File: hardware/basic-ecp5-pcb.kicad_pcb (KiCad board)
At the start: 2 copper layers, 100 x 68 mm, 68 parts, among them J1 Conn_01x02, J2 Conn_02x20_Odd_Even, J3 Conn_02x06_Odd_Even, J4 Conn_02x06_Odd_Even, J5 Conn_02x06_Odd_Even, J6 Conn_02x06_Odd_Even, J7 Conn_02x06_Odd_Even, J8 Conn_02x06_Odd_Even, J9 Conn_02x20_Odd_Even, Q1 Q_NMOS_GSD, SW1 SW_Push, SW2 SW_Push, U1 ECP5U_45_CABGA256, U2 IS25LP016D-JBLE, U3 TLV73312PDBV, U4 TLV73333PDBV, X1 SiT2001B

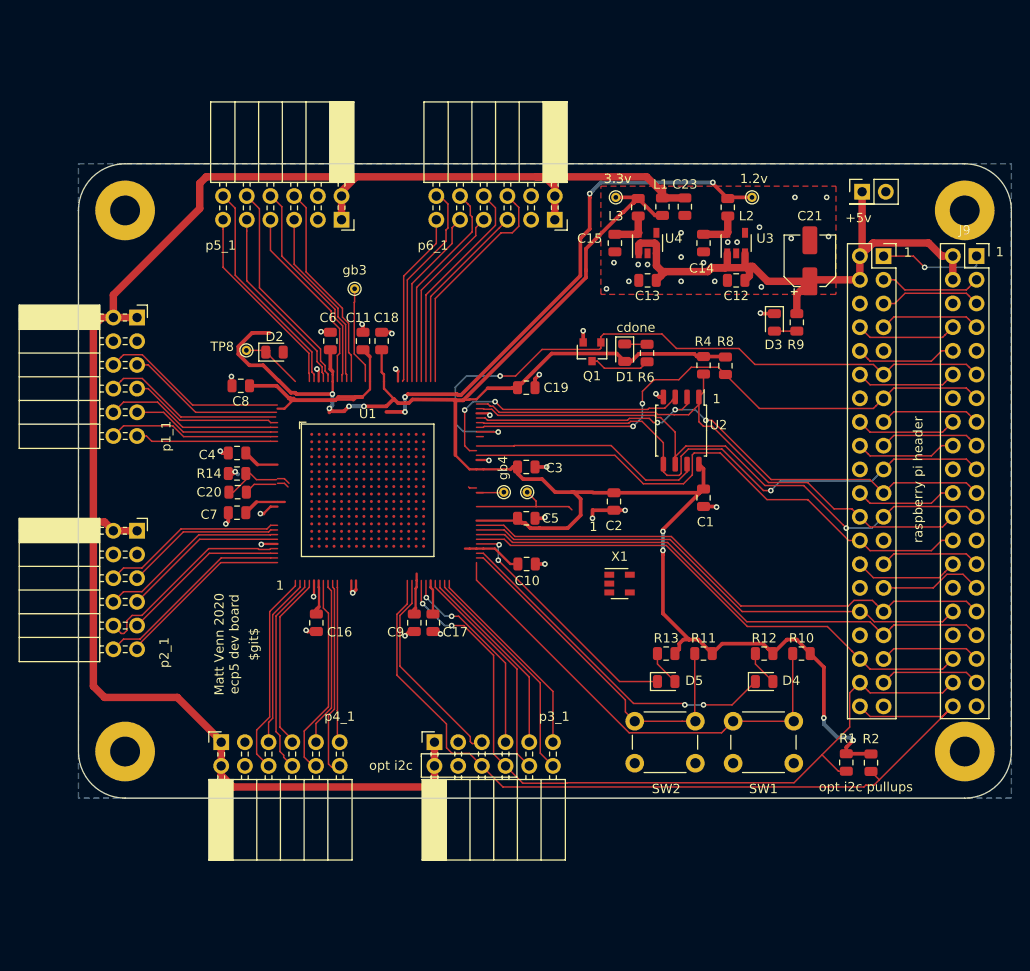
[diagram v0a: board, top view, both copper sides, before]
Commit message: pmods connected and routed
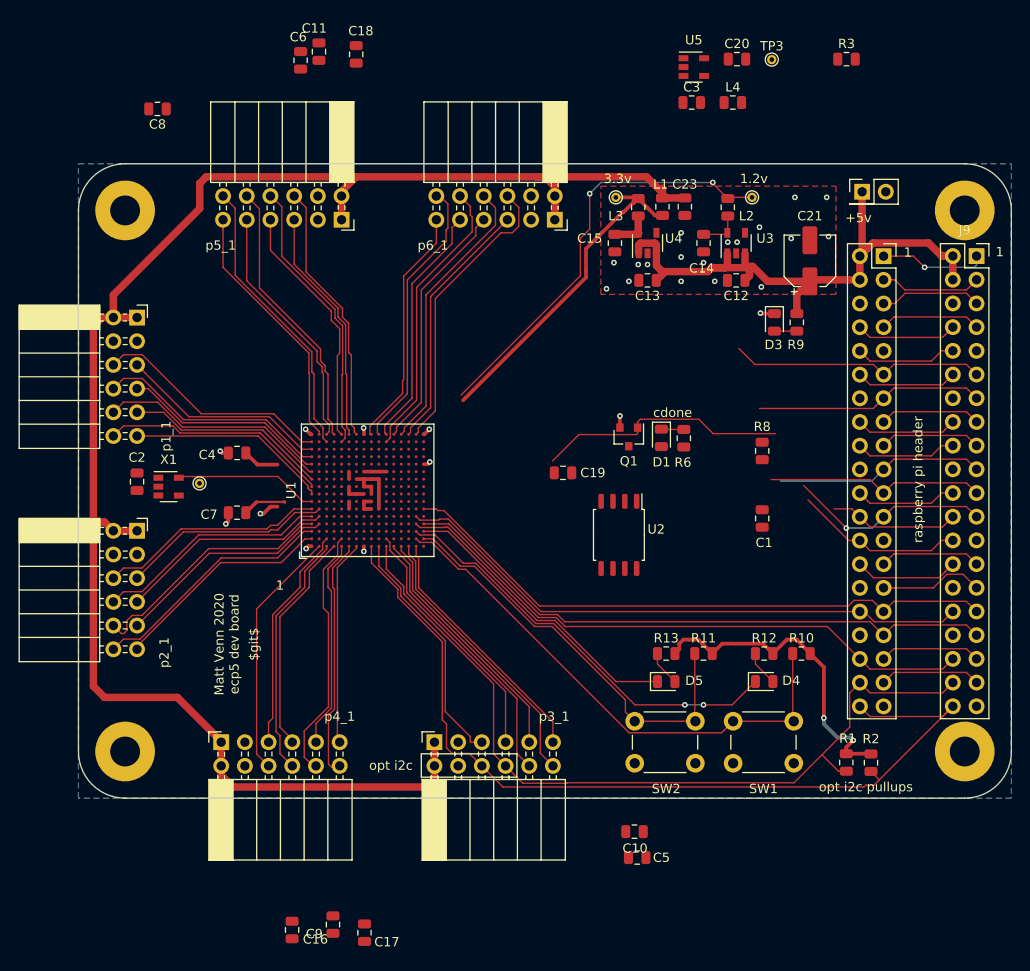
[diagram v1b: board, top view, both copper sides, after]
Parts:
- removed D2: D, Diode_SMD:D_0805_2012Metric
- removed R14: 200R, Resistor_SMD:R_0805_2012Metric
- removed R4: 10k, Resistor_SMD:R_0805_2012Metric
- removed TP1: gbin3, TestPoint:TestPoint_THTPad_D1.0mm_Drill0.5mm
- removed TP2: gbin4, TestPoint:TestPoint_THTPad_D1.0mm_Drill0.5mm
- removed TP8: 2.5v, TestPoint:TestPoint_THTPad_D1.0mm_Drill0.5mm
- added L4: L, Inductor_SMD:L_0805_2012Metric, F.Cu at (145.1, 44.4)
- added R3: 10k, Resistor_SMD:R_0805_2012Metric, F.Cu at (157.3, 39.8)
- added TP3: 2.5v, TestPoint:TestPoint_THTPad_D1.0mm_Drill0.5mm, F.Cu at (149.3, 39.8)
- added U5: TLV73325PDBV, Package_TO_SOT_SMD:SOT-23-5, F.Cu at (141.0, 40.6)
- C20, C3: value 100n -> 1u
- TP6: value 1.2v -> 1.1v
- U3: value TLV73312PDBV -> TLV73311PDBV
- moved C20 70.8 mm to (145.6, 39.8)
- moved C2 51.2 mm to (81.3, 85.1), turned to 90 degrees
- moved X1 49.4 mm to (84.7, 85.6)
- moved C3 42.9 mm to (140.7, 44.4)
- moved C5 38.3 mm to (134.9, 125.4)
- moved TP5 35.1 mm to (88.0, 85.3)
- moved C17 34.0 mm to (105.7, 133.4)
- moved C9 33.5 mm to (102.3, 132.6)
- moved C16 33.0 mm to (97.9, 133.1)
- moved C11 31.4 mm to (100.8, 39.0)
- moved C8 31.0 mm to (83.5, 45.1)
- moved C10 30.9 mm to (134.6, 122.6)
- moved C18 30.9 mm to (104.8, 39.3)
- moved C6 30.3 mm to (98.8, 39.9)
- moved U2 13.0 mm to (132.9, 90.8)
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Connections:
- net +1V2 renamed +1V1
- net /1v2 renamed /1v1
- net Net-(D2-Pad1) renamed +2V5
- net Net-(U1-PadM10) renamed /fpga/tdo
- net Net-(U1-PadR11) renamed /fpga/tdi
- net Net-(U1-PadT10) renamed /fpga/tck
- net Net-(U1-PadT11) renamed /fpga/tms
- C20 pad 1: /vcc_pll -> /2v5
- C20 pad 2: Net-(C20-Pad2) -> GND
- C3 pad 1: +3V3 -> +5V
- D4 pad 1: /led1 -> led1
- D5 pad 1: /led2 -> led2
- J2 pad 11: /cdone -> cdone
- J2 pad 13: /creset -> creset
- J2 pad 19: /gp10 -> sdo
- J2 pad 21: /gp9 -> sdi
- J2 pad 23: /gp11 -> sd_clk
- J2 pad 24: /gp8 -> sd_cs
- J2 pad 31: /gp6 -> gp6
- J2 pad 32: /gp12 -> gp12
- J2 pad 33: /gp13 -> gp13
- J2 pad 36: /gp16 -> gp16
- J2 pad 38: /gp20 -> p3_9
- J2 pad 40: /gp21 -> p3_10
- J3 pad 10: /p1_8 -> p1_8
- J3 pad 11: /p1_1 -> p1_1
- J3 pad 12: /p1_7 -> p1_7
- J3 pad 5: /p1_4 -> p1_4
- J3 pad 6: /p1_10 -> p1_10
- J3 pad 7: /p1_3 -> p1_3
- J3 pad 8: /p1_9 -> p1_9
- J3 pad 9: /p1_2 -> p1_2
- J4 pad 10: /p2_8 -> p2_8
- J4 pad 11: /p2_1 -> p2_1
- J4 pad 12: /p2_7 -> p2_7
- J4 pad 5: /p2_4 -> p2_4
- J4 pad 6: /p2_10 -> p2_10
- J4 pad 7: /p2_3 -> p2_3
- J4 pad 8: /p2_9 -> p2_9
- J4 pad 9: /p2_2 -> p2_2
- J5 pad 10: /p3_8 -> p3_8
- J5 pad 11: /p3_1 -> p3_1
- J5 pad 12: /p3_7 -> p3_7
- J5 pad 5: /p3_4 -> p3_4
- J5 pad 6: /gp21 -> p3_10
- J5 pad 7: /p3_3 -> p3_3
- J5 pad 8: /gp20 -> p3_9
- J5 pad 9: /p3_2 -> p3_2
- J6 pad 10: /p4_8 -> p4_8
- J6 pad 11: /p4_1 -> p4_1
- J6 pad 12: /p4_7 -> p4_7
- J6 pad 5: /p4_4 -> p4_4
- J6 pad 6: /p4_10 -> p4_10
- J6 pad 7: /p4_3 -> p4_3
- J6 pad 8: /p4_9 -> p4_9
- J6 pad 9: /p4_2 -> p4_2
- J7 pad 10: /p5_8 -> p5_8
- J7 pad 11: /p5_1 -> p5_1
- J7 pad 12: /p5_7 -> p5_7
- J7 pad 5: /p5_4 -> p5_4
- J7 pad 6: /p5_10 -> p5_10
- J7 pad 7: /p5_3 -> p5_3
- J7 pad 8: /p5_9 -> p5_9
- J7 pad 9: /p5_2 -> p5_2
- J8 pad 10: /p6_8 -> p6_8
- J8 pad 11: /p6_1 -> p6_1
- J8 pad 12: /p6_7 -> p6_7
- J8 pad 5: /p6_4 -> p6_4
- J8 pad 6: /p6_10 -> p6_10
- J8 pad 7: /p6_3 -> p6_3
- J8 pad 8: /p6_9 -> p6_9
- J8 pad 9: /p6_2 -> p6_2
- J9 pad 11: /cdone -> cdone
- J9 pad 13: /creset -> creset
- J9 pad 19: /gp10 -> sdo
- J9 pad 21: /gp9 -> sdi
- J9 pad 23: /gp11 -> sd_clk
- J9 pad 24: /gp8 -> sd_cs
- J9 pad 31: /gp6 -> gp6
- J9 pad 32: /gp12 -> gp12
- J9 pad 33: /gp13 -> gp13
- J9 pad 36: /gp16 -> gp16
- J9 pad 38: /gp20 -> p3_9
- J9 pad 40: /gp21 -> p3_10
- Q1 pad 1: /cdone -> cdone
- R1 pad 2: /gp20 -> p3_9
- R10 pad 1: /button1 -> button1
- R11 pad 1: /button2 -> button2
- R2 pad 2: /gp21 -> p3_10
- R8 pad 1: /creset -> creset
- SW1 pad 1: /button1 -> button1
- SW2 pad 1: /button2 -> button2
- TP5 pad 1: /clock -> clk
- U1 pad A10: Net-(U1-PadA10) -> p1_2
- U1 pad A11: Net-(U1-PadA11) -> p1_8
- U1 pad A12: Net-(U1-PadA12) -> p1_3
- U1 pad A13: Net-(U1-PadA13) -> p1_9
- U1 pad A14: Net-(U1-PadA14) -> p1_4
- U1 pad A15: Net-(U1-PadA15) -> p1_10
- U1 pad A2: Net-(U1-PadA2) -> p2_1
- U1 pad A3: Net-(U1-PadA3) -> p2_7
- U1 pad A4: Net-(U1-PadA4) -> p2_8
- U1 pad A5: Net-(U1-PadA5) -> p2_9
- U1 pad A6: Net-(U1-PadA6) -> p2_10
- U1 pad A7: Net-(U1-PadA7) -> clk
- U1 pad A8: Net-(U1-PadA8) -> p1_1
- U1 pad A9: Net-(U1-PadA9) -> p1_7
- U1 pad B1: Net-(U1-PadB1) -> p4_10
- U1 pad B16: Net-(U1-PadB16) -> p5_1
- U1 pad B4: Net-(U1-PadB4) -> p2_2
- U1 pad B5: Net-(U1-PadB5) -> p2_3
- U1 pad B6: Net-(U1-PadB6) -> p2_4
- U1 pad C1: Net-(U1-PadC1) -> p4_9
- U1 pad C15: Net-(U1-PadC15) -> p5_7
- U1 pad C16: Net-(U1-PadC16) -> p5_2
- U1 pad C2: Net-(U1-PadC2) -> p4_4
- U1 pad D1: Net-(U1-PadD1) -> p4_3
- U1 pad D16: Net-(U1-PadD16) -> p5_8
- U1 pad E1: Net-(U1-PadE1) -> p4_2
- U1 pad E15: Net-(U1-PadE15) -> p5_9
- U1 pad E16: Net-(U1-PadE16) -> p5_3
- U1 pad E2: Net-(U1-PadE2) -> p4_8
- U1 pad F1: Net-(U1-PadF1) -> p4_7
- U1 pad F16: Net-(U1-PadF16) -> p5_4
- U1 pad G1: Net-(U1-PadG1) -> p4_1
- U1 pad G16: Net-(U1-PadG16) -> p5_10
- U1 pad J1: Net-(U1-PadJ1) -> p3_10
- U1 pad J16: Net-(U1-PadJ16) -> p6_1
- U1 pad K1: Net-(U1-PadK1) -> p3_4
- U1 pad K16: Net-(U1-PadK16) -> p6_7
- U1 pad L1: Net-(U1-PadL1) -> p3_9
- U1 pad L15: Net-(U1-PadL15) -> p6_8
- U1 pad L16: Net-(U1-PadL16) -> p6_2
- U1 pad L2: Net-(U1-PadL2) -> p3_3
- U1 pad M1: Net-(U1-PadM1) -> p3_8
- U1 pad M16: Net-(U1-PadM16) -> p6_3
- U1 pad M7: Net-(U1-PadM7) -> sd_io2
- U1 pad N1: Net-(U1-PadN1) -> p3_2
- U1 pad N10: Net-(U1-PadN10) -> GND
- U1 pad N16: Net-(U1-PadN16) -> p6_9
- U1 pad N7: Net-(U1-PadN7) -> sd_io3
- U1 pad N8: Net-(U1-PadN8) -> sd_cs
- U1 pad N9: Net-(U1-PadN9) -> sd_clk
- U1 pad P1: Net-(U1-PadP1) -> p3_7
- U1 pad P10: Net-(U1-PadP10) -> +3V3
- U1 pad P16: Net-(U1-PadP16) -> p6_4
- U1 pad P9: Net-(U1-PadP9) -> cdone
- U1 pad R1: Net-(U1-PadR1) -> p3_1
- U1 pad R10: Net-(U1-PadR10) -> GND
- U1 pad R16: Net-(U1-PadR16) -> p6_10
- U1 pad R2: Net-(U1-PadR2) -> button1
- U1 pad R3: Net-(U1-PadR3) -> led1
- U1 pad R4: Net-(U1-PadR4) -> gp16
- U1 pad R5: Net-(U1-PadR5) -> gp12
- U1 pad R9: Net-(U1-PadR9) -> creset
- U1 pad T2: Net-(U1-PadT2) -> button2
- U1 pad T3: Net-(U1-PadT3) -> led2
- U1 pad T4: Net-(U1-PadT4) -> gp13
- U1 pad T6: Net-(U1-PadT6) -> gp6
- U1 pad T7: Net-(U1-PadT7) -> sdi
- U1 pad T8: Net-(U1-PadT8) -> sdo
- U2 pad 1: /gp8 -> sd_cs
- U2 pad 2: /gp9 -> sdi
- U2 pad 3: /sd_io2 -> sd_io2
- U2 pad 5: /gp10 -> sdo
- U2 pad 6: /gp11 -> sd_clk
- U2 pad 7: /sd_io3 -> sd_io3
- X1 pad 5: /clock -> clk
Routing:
- net +3V3: track 237.8 -> 85.0 mm, vias 8 -> 2
- net p3_10: track 0.00 -> 96.7 mm
- net /gp21: track 92.4 -> 0.00 mm
- net p3_9: track 0.00 -> 88.4 mm
- net /gp20: track 84.4 -> 0.00 mm, vias 2 -> 0
- net /cdone: track 72.9 -> 0.00 mm, vias 2 -> 0
- net gp6: track 0.00 -> 65.2 mm
- net gp13: track 0.00 -> 65.1 mm
- net gp16: track 0.00 -> 64.5 mm
- net /gp11: track 64.4 -> 0.00 mm, vias 1 -> 0
- net /gp10: track 63.9 -> 0.00 mm, vias 1 -> 0
- net gp12: track 0.00 -> 62.8 mm
- net /gp8: track 62.4 -> 0.00 mm
- net /gp9: track 61.5 -> 0.00 mm, vias 3 -> 0
- net /creset: track 61.1 -> 0.00 mm, vias 2 -> 0
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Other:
- net class Default: clearance 0.16 -> 0.15; trace_width 0.16 -> 0.15
- rule trace_clearance: 0.16 -> 0.15
- rule trace_min: 0.16 -> 0.15
- board text removed: "gb3"
- board text removed: "gb4"

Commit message: routed
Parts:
- removed C16, C17, C18, C19, C9: 100n, Capacitor_SMD:C_0805_2012Metric
- added C22: 100n, Capacitor_SMD:C_0805_2012Metric, F.Cu at (99.0, 95.8)
- added C24: 100n, Capacitor_SMD:C_0805_2012Metric, F.Cu at (97.0, 74.2)
- added C25: 100n, Capacitor_SMD:C_0805_2012Metric, F.Cu at (115.8, 74.6)
- added C26: 100n, Capacitor_SMD:C_0805_2012Metric, F.Cu at (114.8, 95.9)
- added J10: Conn_02x05_Odd_Even, Connector_PinHeader_1.27mm:PinHeader_2x05_P1.27mm_Vertical, F.Cu at (122.4, 82.2)
- added R14: 10k, Resistor_SMD:R_0805_2012Metric, F.Cu at (144.0, 80.5)
- added R4: 10k, Resistor_SMD:R_0805_2012Metric, F.Cu at (130.0, 82.1)
- added R5: 10k, Resistor_SMD:R_0805_2012Metric, F.Cu at (125.6, 82.1)
- added R7: 10k, Resistor_SMD:R_0805_2012Metric, F.Cu at (127.8, 82.1)
- moved R3 61.7 mm to (133.8, 96.8), turned to 180 degrees
- moved C5 55.0 mm to (113.8, 74.6), turned to 90 degrees
- moved C10 50.9 mm to (117.8, 74.5), turned to 90 degrees
- moved C11 49.4 mm to (94.8, 88.0), turned to 180 degrees
- moved C8 37.7 mm to (104.8, 76.2), turned to 90 degrees
- moved C6 37.2 mm to (106.8, 76.2)
- moved C20 32.9 mm to (132.0, 69.7), turned to 270 degrees
- moved TP3 30.6 mm to (134.2, 66.4)
- moved U5 29.4 mm to (136.0, 69.6), turned to 90 degrees
- moved C3 29.2 mm to (136.0, 73.2), turned to 180 degrees
- moved L4 25.4 mm to (132.0, 66.2), turned to 90 degrees
- moved C1 11.6 mm to (138.1, 94.4), turned to 0 degrees
- moved R8 11.5 mm to (138.0, 87.0), turned to 180 degrees
- moved C4 7.66 mm to (97.0, 76.2)
- moved C7 3.69 mm to (94.8, 86.0)
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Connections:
- J2 pad 26: /ce1 -> ce1
- J9 pad 26: /ce1 -> ce1
- R8 pad 1: creset -> +3V3
- R8 pad 2: +3V3 -> sd_cs
- U1 pad N10: GND -> Net-(R7-Pad2)
- U1 pad P10: +3V3 -> Net-(R5-Pad1)
- U1 pad R10: GND -> Net-(R4-Pad2)
- U1 pad T13: Net-(U1-PadT13) -> ce1
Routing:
- net +2V5: track 0.00 -> 103.5 mm, vias 0 -> 8
- net ce1: track 0.00 -> 68.1 mm, vias 0 -> 4
- net sd_clk: track 21.8 -> 77.5 mm, vias 1 -> 5
- net creset: track 24.6 -> 79.9 mm, vias 0 -> 1
- net +1V1: track 46.1 -> 99.9 mm, vias 2 -> 9
- net sd_cs: track 14.0 -> 66.2 mm, vias 0 -> 2
- net sdo: track 22.4 -> 70.5 mm, vias 0 -> 3
- net +3V3: track 85.0 -> 44.7 mm, vias 2 -> 20
- net sdi: track 23.5 -> 63.7 mm, vias 0 -> 2
- net GND: track 22.0 -> 58.7 mm, vias 29 -> 44
- net sd_io3: track 0.00 -> 28.6 mm
- net sd_io2: track 0.00 -> 26.5 mm, vias 0 -> 2
- net Net-(R4-Pad2): track 0.00 -> 22.4 mm, vias 0 -> 2
- net Net-(R7-Pad2): track 0.00 -> 21.9 mm, vias 0 -> 2
- net Net-(R5-Pad1): track 0.00 -> 18.8 mm, vias 0 -> 2
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- added copper zone on In2.Cu, net +3V3
- added copper zone on In1.Cu, net GND
- removed copper zone on B.Cu, net GND
- removed copper zone on F.Cu, net GND
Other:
- copper layers 2 -> 4
- board text added: "1.1v"
- board text added: "2.5v"
- board text added: "3.3"
- board text added: "clk"
- board text added: "jtag"
- board text added: "p1"
- board text added: "p2"
- board text added: "p3"
- board text added: "p4"
- board text added: "p5"
- board text added: "p6"
- board text removed: "1.2v"
- board text removed: "p1_1"
- board text removed: "p2_1"
- board text removed: "p3_1"
- board text removed: "p4_1"
- board text removed: "p5_1"
- board text removed: "p6_1"

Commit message: changes for design review (see readme)
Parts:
- removed C23, C24, C25: 100n, Capacitor_SMD:C_0805_2012Metric
- removed L1, L4: L, Inductor_SMD:L_0805_2012Metric
- removed R14: 10k, Resistor_SMD:R_0805_2012Metric
- removed TP7: 3.3v, TestPoint:TestPoint_THTPad_D1.0mm_Drill0.5mm
- added C9: 100n, Capacitor_SMD:C_0805_2012Metric, F.Cu at (97.0, 95.8)
- added FB1: Ferrite_Bead_Small, Inductor_SMD:L_0805_2012Metric, F.Cu at (153.2, 70.8)
- added FB2: Ferrite_Bead_Small, Inductor_SMD:L_0805_2012Metric, F.Cu at (140.8, 70.8)
- added FB3: Ferrite_Bead_Small, Inductor_SMD:L_0805_2012Metric, F.Cu at (137.8, 54.5)
- added RN1: 10k, Resistor_SMD:R_Array_Concave_4x0603, F.Cu at (127.8, 79.2)
- added RN2: 10k, Resistor_SMD:R_Array_Concave_4x0603, F.Cu at (125.8, 92.0)
- added TP1: 3.3v, TestPoint:TestPoint_THTPad_D1.0mm_Drill0.5mm, F.Cu at (132.0, 68.0)
- C11, C26, C7: value 100n -> 10u
- C12, C13: value 1u -> 4.7u
- C14: value 1u -> 22u
- C15: value 1u -> 10u
- L2, L3: value L -> 2.2uH; footprint Inductor_SMD:L_0805_2012Metric -> Inductor_SMD:L_Taiyo-Yuden_NR-40xx
- R4: value 10k -> 100k
- R5: value 10k -> 120k
- R7: value 10k -> 68k
- R8: value 10k -> 15k
- U3: value TLV73311PDBV -> TLV62568DBV
- U4: value TLV73333PDBV -> TLV62568DBV
- moved R5 30.4 mm to (150.0, 64.0), turned to 0 degrees
- moved R4 28.4 mm to (150.0, 62.0), turned to 180 degrees
- moved C26 28.2 mm to (97.0, 74.0), turned to 180 degrees
- moved R8 23.0 mm to (137.5, 64.0), turned to 0 degrees
- moved R7 22.6 mm to (137.5, 61.8), turned to 180 degrees
- moved R3 18.3 mm to (120.2, 84.6)
- moved L2 16.4 mm to (147.8, 71.8), turned to 180 degrees
- moved L3 16.1 mm to (135.0, 71.8), turned to 180 degrees
- moved C3 15.5 mm to (137.0, 57.8), turned to 270 degrees
- moved U5 14.5 mm to (133.6, 55.2), turned to 180 degrees
- moved D3 14.2 mm to (141.6, 56.2)
- moved R9 14.2 mm to (144.0, 56.2)
- moved TP6 13.9 mm to (144.5, 68.2), turned to 270 degrees
- moved C20 11.3 mm to (133.5, 58.5), turned to 0 degrees
- moved C14 9.09 mm to (146.8, 67.2), turned to 90 degrees
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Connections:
- C1 pad 1: +3V3 -> +3.3VP
- C12 pad 1: +5V -> Net-(C12-Pad1)
- C13 pad 1: +5V -> Net-(C13-Pad1)
- C14 pad 1: /1v1 -> +1V1
- C15 pad 1: /3v3 -> +3.3VP
- C2 pad 1: +3V3 -> +3.3VP
- C20 pad 1: /2v5 -> +2V5
- C3 pad 1: +5V -> Net-(C3-Pad1)
- C4 pad 1: +3V3 -> +3.3VP
- C5 pad 1: +3V3 -> +3.3VP
- C6 pad 1: +3V3 -> +3.3VP
- C7 pad 1: +3V3 -> +3.3VP
- D1 pad 2: +3V3 -> +3.3VP
- J10 pad 1: +3V3 -> +3.3VP
- L2 pad 1: /1v1 -> Net-(L2-Pad1)
- L3 pad 1: /3v3 -> Net-(L3-Pad1)
- L3 pad 2: +3V3 -> +3.3VP
- R1 pad 1: +3V3 -> +3.3VP
- R10 pad 2: +3V3 -> +3.3VP
- R11 pad 2: +3V3 -> +3.3VP
- R12 pad 2: +3V3 -> +3.3VP
- R13 pad 2: +3V3 -> +3.3VP
- R2 pad 1: +3V3 -> +3.3VP
- R3 pad 1: +3V3 -> GND
- R3 pad 2: sd_clk -> /fpga/tck
- R4 pad 1: GND -> Net-(R4-Pad1)
- R4 pad 2: Net-(R4-Pad2) -> +1V1
- R5 pad 1: Net-(R5-Pad1) -> GND
- R5 pad 2: +3V3 -> Net-(R4-Pad1)
- R7 pad 1: GND -> Net-(R7-Pad1)
- R7 pad 2: Net-(R7-Pad2) -> +3.3VP
- R8 pad 1: +3V3 -> GND
- R8 pad 2: sd_cs -> Net-(R7-Pad1)
- U1 pad F10: +3V3 -> +3.3VP
- U1 pad F11: +3V3 -> +3.3VP
- U1 pad F6: +3V3 -> +3.3VP
- U1 pad F7: +3V3 -> +3.3VP
- U1 pad H11: +3V3 -> +3.3VP
- U1 pad H6: +3V3 -> +3.3VP
- U1 pad H7: +3V3 -> +3.3VP
- U1 pad J11: +3V3 -> +3.3VP
- U1 pad J6: +3V3 -> +3.3VP
- U1 pad J7: +3V3 -> +3.3VP
- U1 pad K11: +3V3 -> +3.3VP
- U1 pad L11: +3V3 -> +3.3VP
- U1 pad L6: +3V3 -> +3.3VP
- U1 pad N10: Net-(R7-Pad2) -> Net-(RN1-Pad1)
- U1 pad P10: Net-(R5-Pad1) -> Net-(RN1-Pad2)
- U1 pad R10: Net-(R4-Pad2) -> Net-(RN1-Pad3)
- U2 pad 8: +3V3 -> +3.3VP
- U3 pad 1: +5V -> Net-(C12-Pad1)
- U3 pad 3: +5V -> Net-(L2-Pad1)
- U3 pad 4: Net-(U3-Pad4) -> Net-(C12-Pad1)
- U3 pad 5: /1v1 -> Net-(R4-Pad1)
- U4 pad 1: +5V -> Net-(C13-Pad1)
- U4 pad 3: +5V -> Net-(L3-Pad1)
- U4 pad 4: Net-(U4-Pad4) -> Net-(C13-Pad1)
- U4 pad 5: /3v3 -> Net-(R7-Pad1)
- U5 pad 1: +5V -> Net-(C3-Pad1)
- U5 pad 3: +5V -> Net-(C3-Pad1)
- U5 pad 5: /2v5 -> +2V5
- X1 pad 3: +3V3 -> +3.3VP
- X1 pad 4: +3V3 -> +3.3VP
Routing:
- net +3.3VP: track 179.4 -> 62.3 mm, vias 0 -> 23
- net +3V3: track 44.7 -> 0.00 mm, vias 20 -> 0
- net Net-(RN1-Pad1): track 0.00 -> 25.0 mm, vias 0 -> 2
- net Net-(RN1-Pad3): track 0.00 -> 24.9 mm, vias 0 -> 2
- net Net-(RN1-Pad2): track 0.00 -> 23.8 mm, vias 0 -> 2
- net Net-(R4-Pad2): track 22.4 -> 0.00 mm, vias 2 -> 0
- net cdone: track 70.5 -> 92.8 mm
- net Net-(R7-Pad2): track 21.9 -> 0.00 mm, vias 2 -> 0
- net +1V1: track 99.9 -> 119.8 mm
- net Net-(R5-Pad1): track 18.8 -> 0.00 mm, vias 2 -> 0
- net GND: track 58.7 -> 75.7 mm, vias 44 -> 49
- net +2V5: track 103.5 -> 92.4 mm, vias 8 -> 6
- net Net-(C12-Pad1): track 0.00 -> 11.0 mm, vias 0 -> 2
- net Net-(C13-Pad1): track 0.00 -> 10.5 mm, vias 0 -> 2
- net sd_cs: track 66.2 -> 76.0 mm, vias 2 -> 4
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- added copper zone on In2.Cu, net +3.3VP
- removed copper zone on In2.Cu, net +3V3
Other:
- net class Default: clearance 0.15 -> 0.13; via_dia 0.6 -> 0.5; via_drill 0.3 -> 0.254
- net class power: clearance 0.16 -> 0.13; via_dia 0.6 -> 0.5; via_drill 0.3 -> 0.4
- net class power5: clearance 0.16 -> 0.13
- rule trace_clearance: 0.15 -> 0.13
- rule via_min_drill: 0.3 -> 0.25

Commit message: tidying
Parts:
- moved C5 2.00 mm to (115.8, 74.5)
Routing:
- net cdone: track 92.8 -> 69.0 mm
- net +2V5: track 92.4 -> 89.3 mm
- net sd_clk: track 75.1 -> 77.3 mm
- net creset: track 83.2 -> 81.3 mm, vias 3 -> 1
- net sd_cs: track 76.0 -> 77.7 mm
- net +1V1: track 119.8 -> 120.9 mm, vias 9 -> 10
- net Net-(RN1-Pad3): track 24.9 -> 23.9 mm
- net ce1: track 68.0 -> 67.0 mm
- net Net-(RN1-Pad2): track 23.8 -> 24.5 mm
- net Net-(RN1-Pad1): track 25.0 -> 24.5 mm
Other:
- net class power: via_dia 0.5 -> 0.6; via_drill 0.4 -> 0.3
